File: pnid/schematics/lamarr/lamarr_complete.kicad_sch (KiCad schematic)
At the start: 72 parts

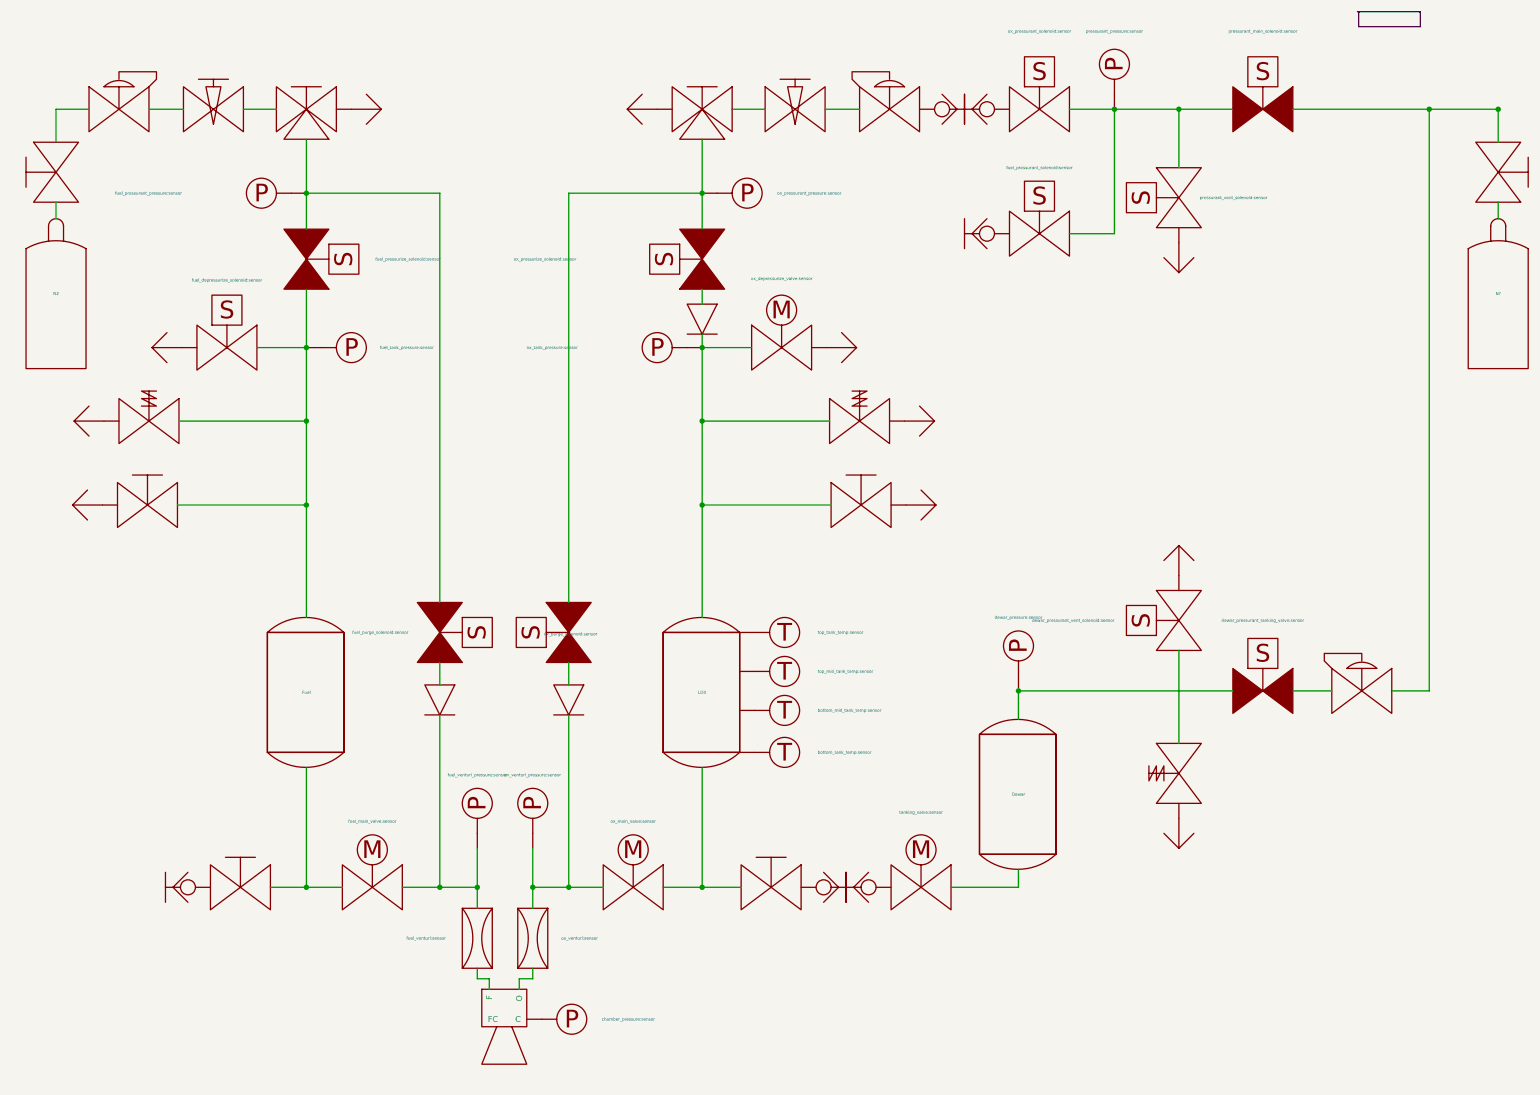
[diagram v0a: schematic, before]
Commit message: update pnids to kicad 8
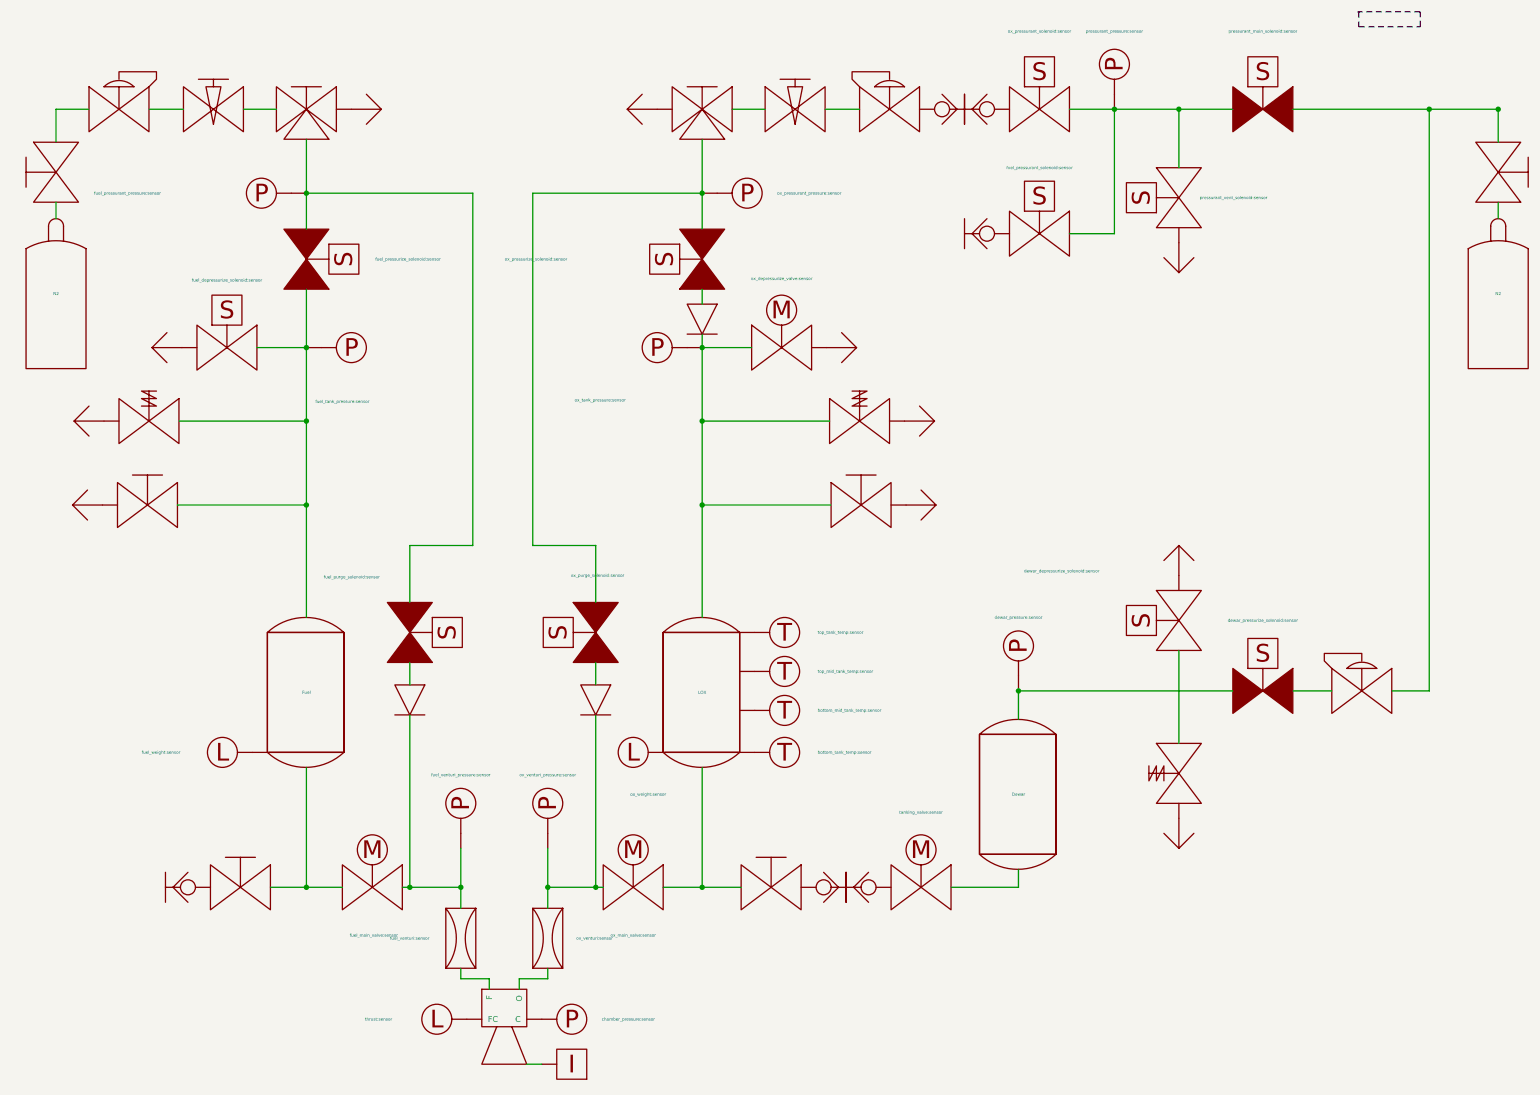
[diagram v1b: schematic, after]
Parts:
- removed Vent?: Vent, symbol PnID-Lib:Vent
- added Vent?: Vent, symbol lamarr_complete-rescue:Vent-PnID-Lib
- added fuel_weight: fuel_weight:sensor, symbol lamarr_complete-rescue:Sensor_Load-PnID-Lib
- added igniter: igniter:sensor, symbol lamarr_complete-rescue:igniter-PnID-Lib
- added ox_weight: ox_weight:sensor, symbol lamarr_complete-rescue:Sensor_Load_Short-PnID-Lib
- added thrust: thrust:sensor, symbol lamarr_complete-rescue:Sensor_Load-PnID-Lib
- CheckValve? (x3): symbol PnID-Lib:CheckValve -> lamarr_complete-rescue:CheckValve-PnID-Lib
- Dewar, Fuel, LOX: symbol PnID-Lib:Tank_Slim -> lamarr_complete-rescue:Tank_Slim-PnID-Lib
- DewarOverPressureValve?, fuel_safety_valve, ox_safety_valve: symbol PnID-Lib:Valve_OverPressure -> lamarr_complete-rescue:Valve_OverPressure-PnID-Lib
- DewarPressureRegulator?, fuel_pressure_regulator, ox_pressure_regulator: symbol PnID-Lib:PressureRegulator -> lamarr_complete-rescue:PressureRegulator-PnID-Lib
- DewarQuickConnect?, QuickConnect?, fuel_quick_connect, fuel_quick_connect?, ox_quick_connect, ox_quick_connect?: symbol PnID-Lib:QuickConnect_Half -> lamarr_complete-rescue:QuickConnect_Half-PnID-Lib
- N2: symbol PnID-Lib:GasBottle -> lamarr_complete-rescue:GasBottle-PnID-Lib
- N2: renamed from N?; symbol PnID-Lib:GasBottle -> lamarr_complete-rescue:GasBottle-PnID-Lib
- Vent? (x10): symbol PnID-Lib:Vent -> lamarr_complete-rescue:Vent-PnID-Lib
- bottom_mid_tank_temp, bottom_tank_temp, top_mid_tank_temp, top_tank_temp: symbol PnID-Lib:Sensor_Temperature -> lamarr_complete-rescue:Sensor_Temperature-PnID-Lib
- chamber_pressure, dewar_pressure?, fuel_pressurant_pressure, fuel_tank_pressure, fuel_venturi_pressure, ox_pressurant_pressure:sensor, ox_tank_pressure, ox_venturi_pressure, pressurant_pressure?: symbol PnID-Lib:Sensor_Pressure -> lamarr_complete-rescue:Sensor_Pressure-PnID-Lib
- dewar_depressurize_solenoid?: renamed from dewar_pressurant_vent_solenoid?; value dewar_pressurant_vent_solenoid:sensor -> dewar_depressurize_solenoid:sensor; symbol PnID-Lib:Valve_Solenoid_NO -> lamarr_complete-rescue:Valve_Solenoid_NO-PnID-Lib
- dewar_pressurize_solenoid?: renamed from dewar_pressurant_tanking_valve?; value dewar_pressurant_tanking_valve:sensor -> dewar_pressurize_solenoid:sensor; symbol PnID-Lib:Valve_Solenoid_NC -> lamarr_complete-rescue:Valve_Solenoid_NC-PnID-Lib
- engine: symbol PnID-Lib:Engine -> lamarr_complete-rescue:Engine-PnID-Lib
- fuel_depressurize_solenoid, fuel_pressurant_solenoid?, ox_pressurant_solenoid?, pressurant_vent_solenoid?: symbol PnID-Lib:Valve_Solenoid_NO -> lamarr_complete-rescue:Valve_Solenoid_NO-PnID-Lib
- fuel_main_valve, ox_depressurize_valve, ox_main_valve, tanking_valve?: symbol PnID-Lib:Valve_Servo -> lamarr_complete-rescue:Valve_Servo-PnID-Lib
- fuel_manual_3way, fuel_manual_3way?: symbol PnID-Lib:Valve_Manual_3Way -> lamarr_complete-rescue:Valve_Manual_3Way-PnID-Lib
- fuel_manual_tanking_valve, fuel_manual_valve, fuel_manual_vent_valve, ox_manual_tanking_valve, ox_manual_valve, ox_manual_vent_valve: symbol PnID-Lib:Valve_Manual -> lamarr_complete-rescue:Valve_Manual-PnID-Lib
- fuel_needle_valve, ox_needle_valve: symbol PnID-Lib:Valve_Needle -> lamarr_complete-rescue:Valve_Needle-PnID-Lib
- fuel_pressurize_solenoid, fuel_purge_solenoid, ox_pressurize_solenoid, ox_purge_solenoid, pressurant_main_solenoid?: symbol PnID-Lib:Valve_Solenoid_NC -> lamarr_complete-rescue:Valve_Solenoid_NC-PnID-Lib
- fuel_venturi, ox_venturi: symbol PnID-Lib:Venturi -> lamarr_complete-rescue:Venturi-PnID-Lib
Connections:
- net at engine.~ (O): now also thrust.~
- net at ox_venturi.~: now also CheckValve?.~, ox_main_valve.~, ox_venturi_pressure.~; no longer engine.~ (O)
- net at fuel_venturi.~: now also CheckValve?.~, fuel_main_valve.~, fuel_venturi_pressure.~; no longer engine.~ (O)
- net at DewarPressureRegulator?.~: now also ox_manual_valve.~, pressurant_main_solenoid?.~; no longer dewar_pressurize_solenoid?.~
- net at DewarOverPressureValve?.~: now also Vent?.~; no longer dewar_depressurize_solenoid?.~
- net at ox_manual_vent_valve.~: now also Vent?.~
- new net: fuel_manual_3way?.~, ox_pressurant_pressure:sensor.~, ox_pressurize_solenoid.~, ox_purge_solenoid.~
- new net: fuel_manual_3way.~, fuel_pressurant_pressure.~, fuel_pressurize_solenoid.~, fuel_purge_solenoid.~
- new net: Fuel.~, fuel_depressurize_solenoid.~, fuel_manual_vent_valve.~, fuel_pressurize_solenoid.~, fuel_safety_valve.~, fuel_tank_pressure.~
- new net: CheckValve?.~, LOX.~, ox_depressurize_valve.~, ox_manual_vent_valve.~, ox_safety_valve.~, ox_tank_pressure.~
- new net: LOX.~, ox_main_valve.~, ox_manual_tanking_valve.~
- new net: Fuel.~, fuel_main_valve.~, fuel_manual_tanking_valve.~
- new net: engine.~ (O), ox_venturi.~
- new net: engine.~ (O), fuel_venturi.~
- new net: DewarPressureRegulator?.~, dewar_pressurize_solenoid?.~
- new net: DewarOverPressureValve?.~, dewar_depressurize_solenoid?.~
- new net: fuel_pressurant_solenoid?.~, ox_pressurant_solenoid?.~, pressurant_main_solenoid?.~, pressurant_pressure?.~, pressurant_vent_solenoid?.~

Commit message: fix symbol library connection for lamarr_complete pnid
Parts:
- CheckValve? (x3): symbol lamarr_complete-rescue:CheckValve-PnID-Lib -> PnID-Lib:CheckValve
- Dewar, Fuel, LOX: symbol lamarr_complete-rescue:Tank_Slim-PnID-Lib -> PnID-Lib:Tank_Slim
- DewarOverPressureValve?, fuel_safety_valve, ox_safety_valve: symbol lamarr_complete-rescue:Valve_OverPressure-PnID-Lib -> PnID-Lib:Valve_OverPressure
- DewarPressureRegulator?, fuel_pressure_regulator, ox_pressure_regulator: symbol lamarr_complete-rescue:PressureRegulator-PnID-Lib -> PnID-Lib:PressureRegulator
- DewarQuickConnect?, QuickConnect?, fuel_quick_connect, fuel_quick_connect?, ox_quick_connect, ox_quick_connect?: symbol lamarr_complete-rescue:QuickConnect_Half-PnID-Lib -> PnID-Lib:QuickConnect_Half
- N2: symbol lamarr_complete-rescue:GasBottle-PnID-Lib -> PnID-Lib:GasBottle
- Vent? (x11): symbol lamarr_complete-rescue:Vent-PnID-Lib -> PnID-Lib:Vent
- bottom_mid_tank_temp, bottom_tank_temp, top_mid_tank_temp, top_tank_temp: symbol lamarr_complete-rescue:Sensor_Temperature-PnID-Lib -> PnID-Lib:Sensor_Temperature
- chamber_pressure, dewar_pressure?, fuel_pressurant_pressure, fuel_tank_pressure, fuel_venturi_pressure, ox_pressurant_pressure:sensor, ox_tank_pressure, ox_venturi_pressure, pressurant_pressure?: symbol lamarr_complete-rescue:Sensor_Pressure-PnID-Lib -> PnID-Lib:Sensor_Pressure
- dewar_depressurize_solenoid?, fuel_depressurize_solenoid, fuel_pressurant_solenoid?, ox_pressurant_solenoid?, pressurant_vent_solenoid?: symbol lamarr_complete-rescue:Valve_Solenoid_NO-PnID-Lib -> PnID-Lib:Valve_Solenoid_NO
- dewar_pressurize_solenoid?, fuel_pressurize_solenoid, fuel_purge_solenoid, ox_pressurize_solenoid, ox_purge_solenoid, pressurant_main_solenoid?: symbol lamarr_complete-rescue:Valve_Solenoid_NC-PnID-Lib -> PnID-Lib:Valve_Solenoid_NC
- engine: symbol lamarr_complete-rescue:Engine-PnID-Lib -> PnID-Lib:Engine
- fuel_main_valve, ox_depressurize_valve, ox_main_valve, tanking_valve?: symbol lamarr_complete-rescue:Valve_Servo-PnID-Lib -> PnID-Lib:Valve_Servo
- fuel_manual_3way, fuel_manual_3way?: symbol lamarr_complete-rescue:Valve_Manual_3Way-PnID-Lib -> PnID-Lib:Valve_Manual_3Way
- fuel_manual_tanking_valve, fuel_manual_valve, fuel_manual_vent_valve, ox_manual_tanking_valve, ox_manual_valve, ox_manual_vent_valve: symbol lamarr_complete-rescue:Valve_Manual-PnID-Lib -> PnID-Lib:Valve_Manual
- fuel_needle_valve, ox_needle_valve: symbol lamarr_complete-rescue:Valve_Needle-PnID-Lib -> PnID-Lib:Valve_Needle
- fuel_venturi, ox_venturi: symbol lamarr_complete-rescue:Venturi-PnID-Lib -> PnID-Lib:Venturi
- fuel_weight, thrust: symbol lamarr_complete-rescue:Sensor_Load-PnID-Lib -> PnID-Lib:Sensor_Load_Short
- igniter: symbol lamarr_complete-rescue:igniter-PnID-Lib -> PnID-Lib:igniter
- ox_weight: symbol lamarr_complete-rescue:Sensor_Load_Short-PnID-Lib -> PnID-Lib:Sensor_Load_Short
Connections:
- net at engine.~ (O): now also thrust.~; no longer ox_venturi.~
- net at fuel_venturi.~: now also CheckValve?.~, fuel_main_valve.~, fuel_venturi_pressure.~; no longer engine.~ (O)
- net at Vent?.~: now also fuel_manual_3way?.; no longer fuel_manual_3way?.~
- net at Vent?.~: now also fuel_manual_3way.; no longer fuel_manual_3way.~
- net at fuel_needle_valve.~: now also fuel_manual_3way.; no longer fuel_manual_3way.~
- net at DewarPressureRegulator?.~: now also ox_manual_valve.~, pressurant_main_solenoid?.~; no longer dewar_pressurize_solenoid?.~
- net at DewarOverPressureValve?.~: now also Vent?.~; no longer dewar_depressurize_solenoid?.~
- net at ox_needle_valve.~: now also fuel_manual_3way?.; no longer fuel_manual_3way?.~
- new net: fuel_manual_3way?., ox_pressurant_pressure:sensor.~, ox_pressurize_solenoid.~, ox_purge_solenoid.~
- new net: fuel_manual_3way., fuel_pressurant_pressure.~, fuel_pressurize_solenoid.~, fuel_purge_solenoid.~
- new net: Fuel.~, fuel_depressurize_solenoid.~, fuel_manual_vent_valve.~, fuel_pressurize_solenoid.~, fuel_safety_valve.~, fuel_tank_pressure.~
- new net: CheckValve?.~, LOX.~, ox_depressurize_valve.~, ox_manual_vent_valve.~, ox_safety_valve.~, ox_tank_pressure.~
- new net: LOX.~, ox_main_valve.~, ox_manual_tanking_valve.~
- new net: Fuel.~, fuel_main_valve.~, fuel_manual_tanking_valve.~
- new net: engine.~ (O), ox_venturi.~
- new net: engine.~ (O), fuel_venturi.~
- new net: DewarPressureRegulator?.~, dewar_pressurize_solenoid?.~
- new net: DewarOverPressureValve?.~, dewar_depressurize_solenoid?.~
- new net: fuel_pressurant_solenoid?.~, ox_pressurant_solenoid?.~, pressurant_main_solenoid?.~, pressurant_pressure?.~, pressurant_vent_solenoid?.~
